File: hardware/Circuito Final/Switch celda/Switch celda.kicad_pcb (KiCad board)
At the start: 2 copper layers, 17 parts, among them Q1 MMBT2222A, Q2 MMBT2907A, Q3 MMBT2222A

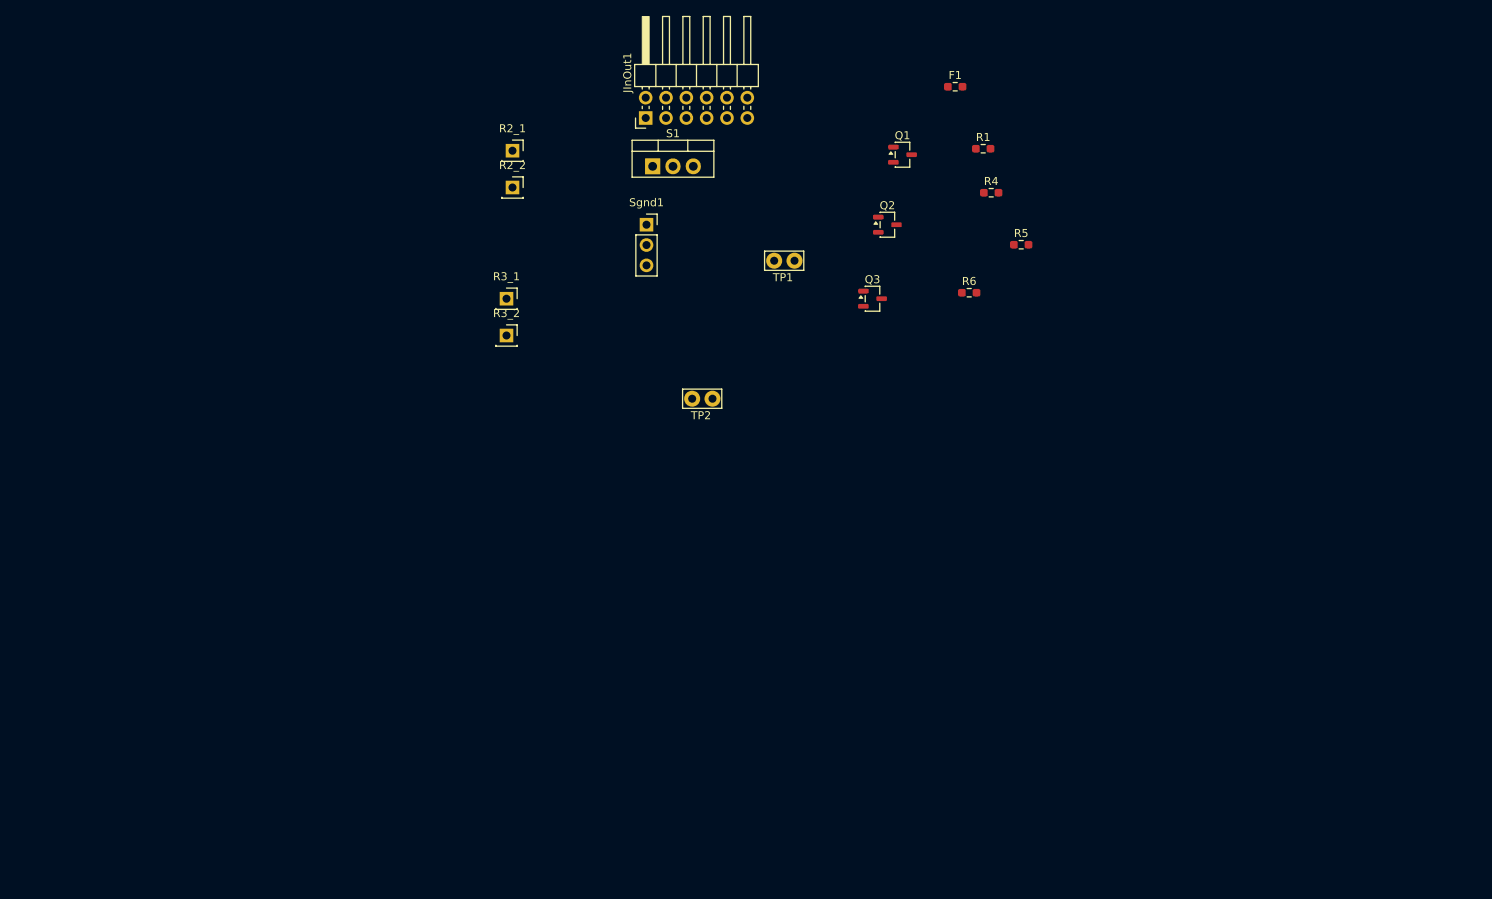
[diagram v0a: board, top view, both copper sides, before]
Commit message: Finalización del esquemático de la celda y subida de datasheets nuevas
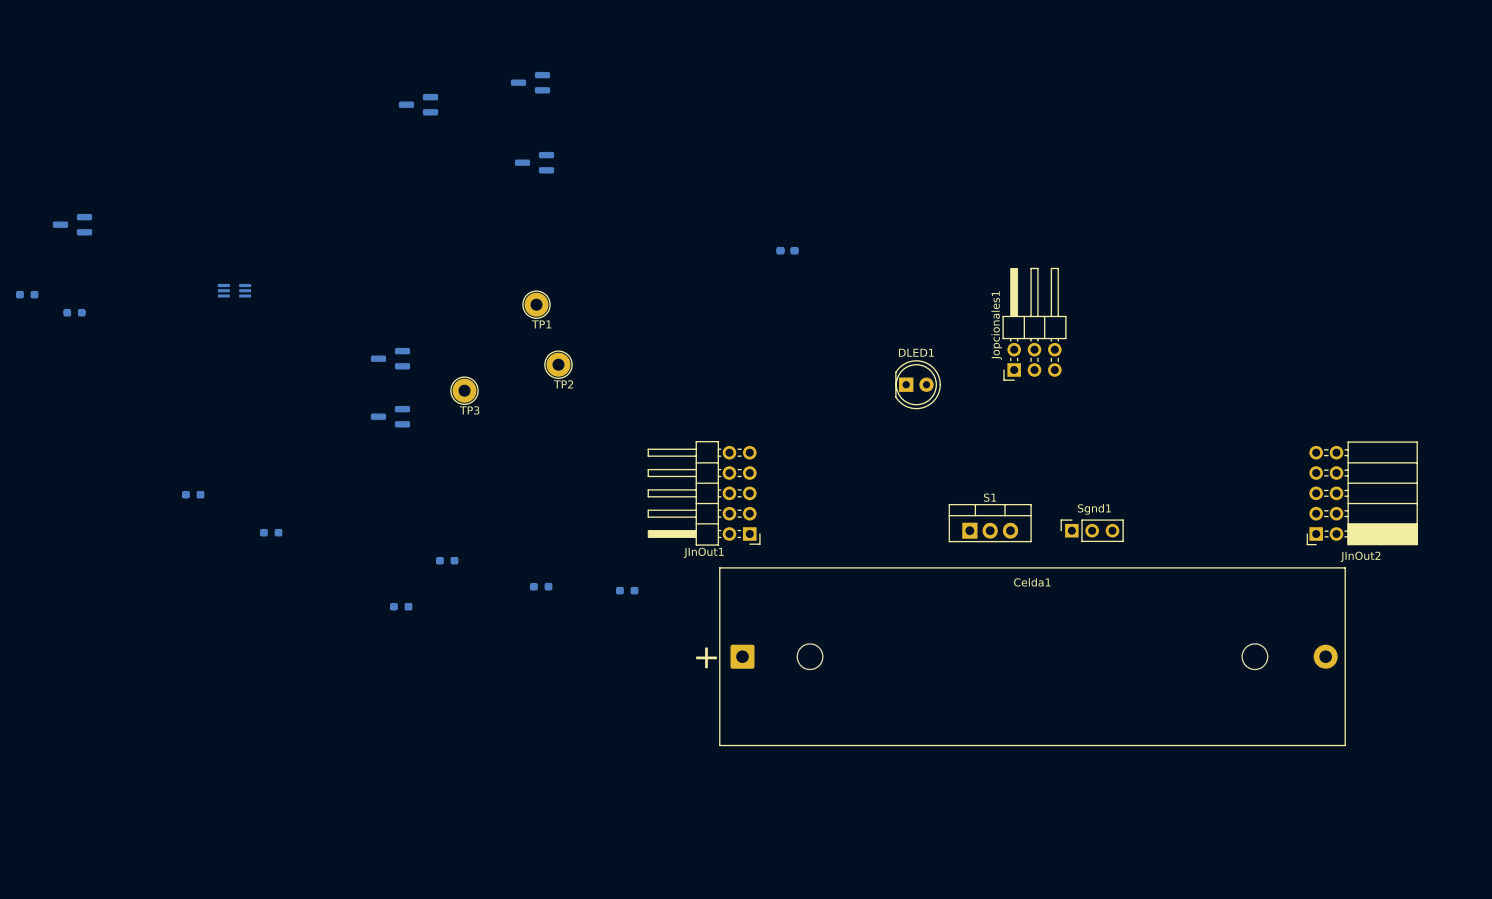
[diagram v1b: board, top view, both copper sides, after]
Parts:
- removed R2_1, R2_2, R3_1, R3_2: Conn_01x01_Socket, Connector_PinSocket_2.54mm:PinSocket_1x01_P2.54mm_Vertical
- added Celda1: Portapilas 18650, Battery:BatteryHolder_MPD_BK-18650-PC2, F.Cu at (143.0, 132.5)
- added DLED1: LED, LED_THT:LED_D5.0mm, F.Cu at (163.5, 98.5)
- added JInOut2: Conn_02x05_Odd_Even, Connector_PinSocket_2.54mm:PinSocket_2x05_P2.54mm_Horizontal, F.Cu at (214.7, 117.2)
- added Jopcionales1: Conn_02x03_Odd_Even, Connector_PinHeader_2.54mm:PinHeader_2x03_P2.54mm_Horizontal, F.Cu at (177.0, 96.7)
- added QLED1: MMBT2222A, Package_TO_SOT_SMD:SOT-23_Handsoldering, B.Cu at (59.2, 78.5)
- added Qinv1: AO3401, Package_TO_SOT_SMD:SOT-23_Handsoldering, B.Cu at (99.0, 95.2)
- added Qinv2: AO3400, Package_TO_SOT_SMD:SOT-23_Handsoldering, B.Cu at (99.0, 102.5)
- added R2: TBD, Resistor_SMD:R_0603_1608Metric_Pad0.98x0.95mm_HandSolder, B.Cu at (84.1, 117.0)
- added R3: TBD, Resistor_SMD:R_0603_1608Metric_Pad0.98x0.95mm_HandSolder, B.Cu at (100.3, 126.2)
- added RLED1: 20k, Resistor_SMD:R_0603_1608Metric_Pad0.98x0.95mm_HandSolder, B.Cu at (59.5, 89.5)
- added RLED2: 1k, Resistor_SMD:R_0603_1608Metric_Pad0.98x0.95mm_HandSolder, B.Cu at (53.6, 87.2)
- added TP3: TP_inv, TestPoint:TestPoint_Loop_D2.54mm_Drill1.5mm_Beaded, F.Cu at (108.2, 99.2)
- added U1: 74LVC1G157, Package_TO_SOT_SMD:SOT-363_SC-70-6_Handsoldering, B.Cu at (79.5, 86.8)
- F1: value Fuse -> ~; footprint Resistor_SMD:R_0603_1608Metric_Pad0.98x0.95mm_HandSolder -> Fuse:Fuse_0603_1608Metric_Pad1.05x0.95mm_HandSolder; moved to B.Cu
- JInOut1: value Conn_02x06_Row_Letter_Last -> Conn_02x05_Odd_Even; footprint Connector_PinHeader_2.54mm:PinHeader_2x06_P2.54mm_Horizontal -> Connector_PinHeader_2.54mm:PinHeader_2x05_P2.54mm_Horizontal
- Q1, Q2, Q3: footprint Package_TO_SOT_SMD:SOT-23-3 -> Package_TO_SOT_SMD:SOT-23_Handsoldering; moved to B.Cu
- R1, R4, R5, R6: moved to B.Cu
- TP1, TP2: footprint TestPoint:TestPoint_Bridge_Pitch2.54mm_Drill1.0mm -> TestPoint:TestPoint_Loop_D2.54mm_Drill1.5mm_Beaded
- moved R1 107.8 mm to (74.3, 112.2), turned to 180 degrees
- moved R4 82.1 mm to (106.1, 120.5), turned to 180 degrees
- moved R5 73.7 mm to (117.8, 123.8), turned to 180 degrees
- moved Sgnd1 65.5 mm to (184.2, 116.8), turned to 90 degrees
- moved Q1 60.8 mm to (102.5, 63.5), turned to 180 degrees
- moved S1 60.4 mm to (171.4, 116.8)
- moved R6 56.7 mm to (128.6, 124.2), turned to 180 degrees
- moved JInOut1 53.6 mm to (143.9, 117.2), turned to 180 degrees
- moved Q2 48.0 mm to (116.5, 60.8), turned to 180 degrees
- moved Q3 45.5 mm to (117.0, 70.8), turned to 180 degrees
- moved TP1 30.2 mm to (117.2, 88.5)
- moved F1 29.3 mm to (148.6, 81.8), turned to 180 degrees
- moved TP2 17.2 mm to (120.0, 96.0)
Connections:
- F1 pad 1: Net-(S1-D) -> Net-(Celda1-+)
- F1 pad 2: bus_neg -> bus_pos
- JInOut1 pad 1: Vcell -> Vcc
- JInOut1 pad 10: bus_neg -> 0
- JInOut1 pad 2: Vcell -> Vcc
- JInOut1 pad 3: Vcell_neg -> Vcell_banco
- JInOut1 pad 4: Vcell_neg -> Vcell_banco
- JInOut1 pad 7: cell_neg -> bus_neg
- JInOut1 pad 8: cell_neg -> bus_neg
- JInOut1 pad 9: bus_neg -> 0
- R1 pad 1: Vcell -> Vin
- R6 pad 1: Vcell_neg -> Net-(Qinv1-D)
- S1 pad 1: Net-(S1-D) -> bus_neg

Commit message: Update PCB celda
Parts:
- moved QLED1 105.2 mm to (143.9, 140.9)
- moved RLED2 102.4 mm to (143.0, 137.1)
- moved Q3 100.5 mm to (190.4, 139.3)
- moved RLED1 99.8 mm to (147.2, 137.2)
- moved Q2 90.7 mm to (177.8, 127.7)
- moved R2 85.0 mm to (168.7, 125.0)
- moved TP3 84.9 mm to (191.3, 117.0)
- moved Q1 84.9 mm to (160.8, 125.2)
- moved Qinv2 80.0 mm to (170.8, 137.8)
- moved R1 78.0 mm to (151.5, 123.8)
- moved Qinv1 77.4 mm to (163.2, 138.3)
- moved U1 73.7 mm to (143.1, 124.1), turned to 0 degrees
- moved TP1 73.1 mm to (184.6, 117.0)
- moved R3 68.4 mm to (168.7, 129.5)
- moved R6 56.6 mm to (183.4, 138.2)
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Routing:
- net Vcell_banco: track 0.00 -> 16.0 mm
- net Vcc: track 0.00 -> 11.1 mm
- net Vcell: track 0.00 -> 10.2 mm
- net Net-(DLED1-K): track 0.00 -> 8.07 mm
- net Net-(QLED1-C): track 0.00 -> 7.68 mm
- net Net-(QLED1-B): track 0.00 -> 5.11 mm
- net bus_pos: track 0.00 -> 5.08 mm
- net bus_neg: track 0.00 -> 5.08 mm
- net 0: track 0.00 -> 5.08 mm
- net cell_neg: track 0.00 -> 2.54 mm
- net Vcell_enable: track 0.00 -> 2.54 mm

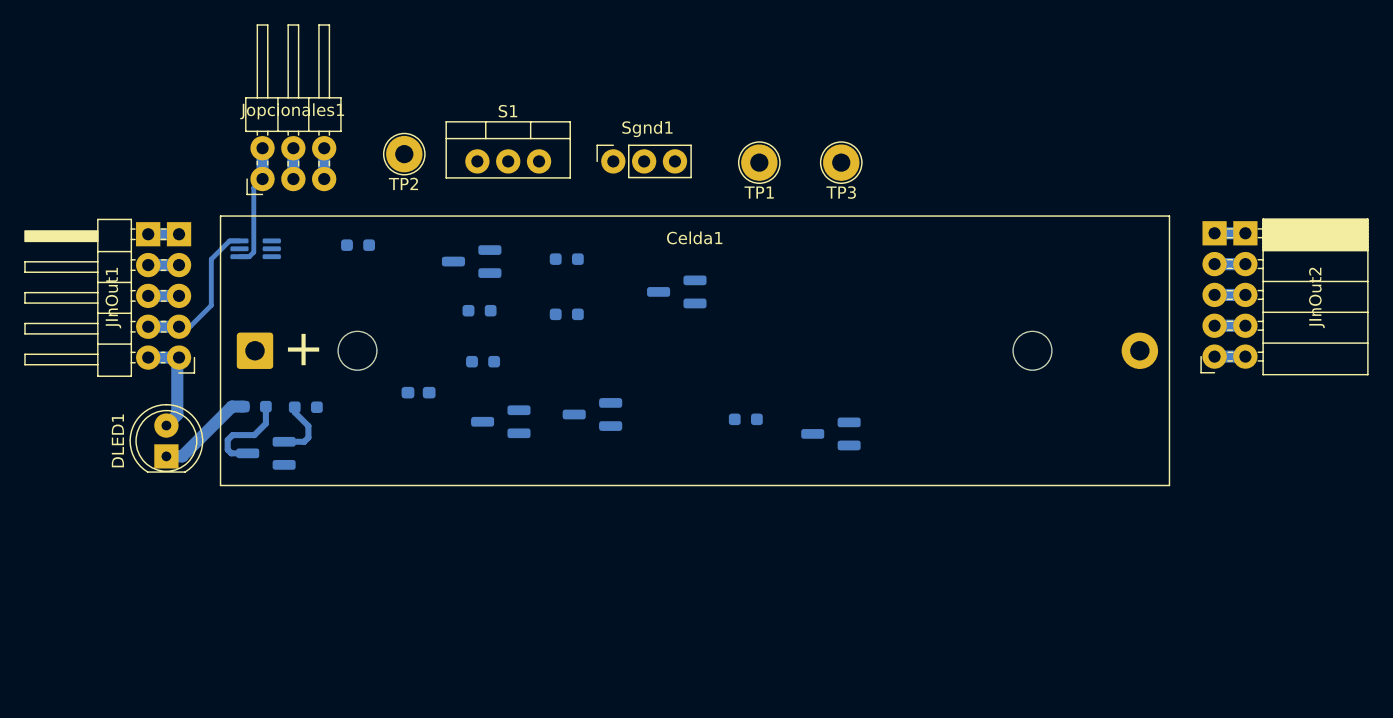
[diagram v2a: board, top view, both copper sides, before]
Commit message: Update PCB celda completo - Revisar integridad
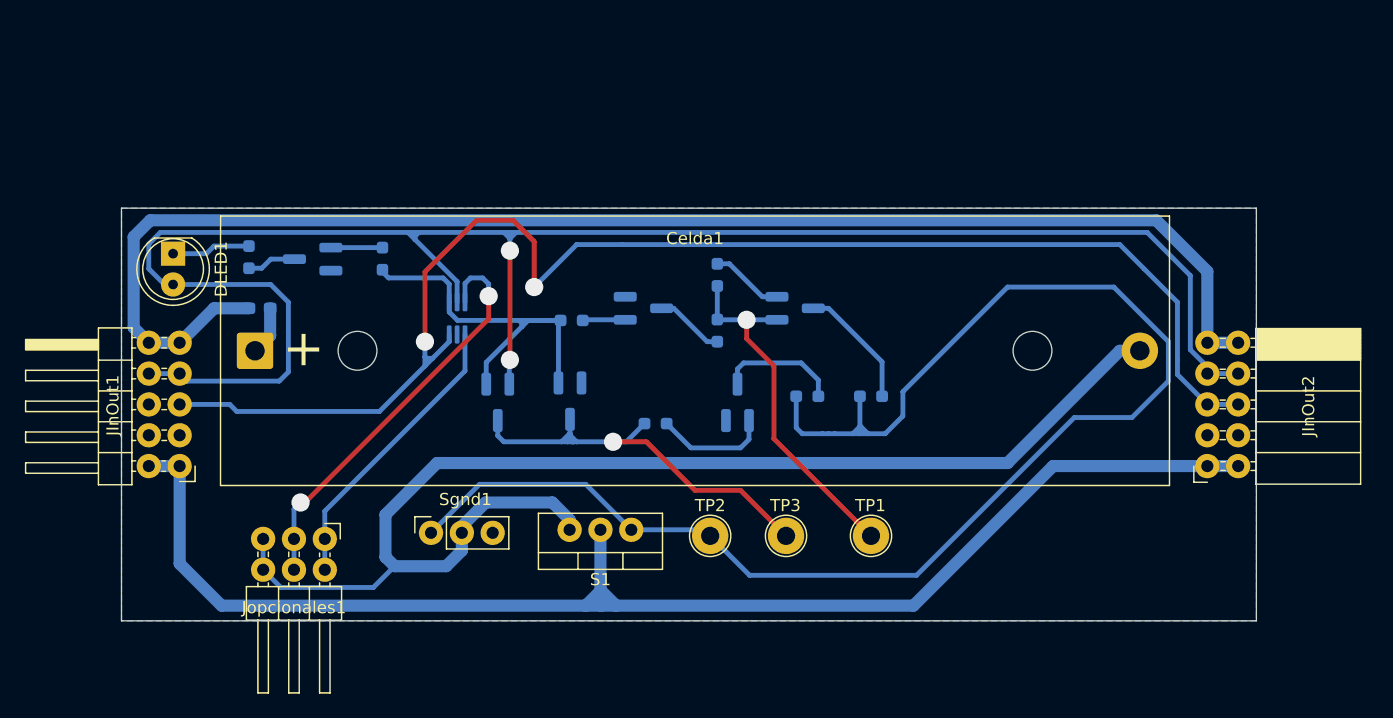
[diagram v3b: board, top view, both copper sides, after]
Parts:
- moved TP2 40.3 mm to (180.5, 147.8), turned to 180 degrees
- moved Sgnd1 34.1 mm to (157.5, 147.5)
- moved R4 33.0 mm to (193.8, 136.2), turned to 0 degrees
- moved S1 32.9 mm to (174.0, 147.2), turned to 180 degrees
- moved TP1 32.1 mm to (193.8, 147.8), turned to 180 degrees
- moved TP3 31.1 mm to (186.8, 147.8), turned to 180 degrees
- moved Jopcionales1 30.1 mm to (148.8, 148.0), turned to -90 degrees
- moved R5 26.9 mm to (188.5, 136.2)
- moved R1 18.7 mm to (169.1, 130.0), turned to 0 degrees
- moved U1 17.6 mm to (159.7, 129.8), turned to 90 degrees
- moved DLED1 16.7 mm to (136.2, 124.5), turned to -90 degrees
- moved QLED1 16.5 mm to (147.8, 125.0)
- moved F1 14.8 mm to (143.4, 129.0)
- moved Q1 14.7 mm to (175.0, 129.0), turned to 0 degrees
- moved RLED1 13.8 mm to (153.5, 124.9), turned to 90 degrees
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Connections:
- JInOut1 pad 1: Vcc -> bus_neg
- JInOut1 pad 10: 0 -> bus_pos
- JInOut1 pad 2: Vcc -> bus_neg
- JInOut1 pad 3: Vcell_banco -> 0
- JInOut1 pad 4: Vcell_banco -> 0
- JInOut1 pad 5: bus_pos -> Vcell_banco
- JInOut1 pad 6: bus_pos -> Vcell_banco
- JInOut1 pad 7: bus_neg -> Vcc
- JInOut1 pad 8: bus_neg -> Vcc
- JInOut1 pad 9: 0 -> bus_pos
- JInOut2 pad 1: Vcc -> bus_neg
- JInOut2 pad 10: 0 -> bus_pos
- JInOut2 pad 2: Vcc -> bus_neg
- JInOut2 pad 3: Vcell_banco -> 0
- JInOut2 pad 4: Vcell_banco -> 0
- JInOut2 pad 5: bus_pos -> Vcell_banco
- JInOut2 pad 6: bus_pos -> Vcell_banco
- JInOut2 pad 7: bus_neg -> Vcc
- JInOut2 pad 8: bus_neg -> Vcc
- JInOut2 pad 9: 0 -> bus_pos
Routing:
- net Vcc: track 11.1 -> 153.4 mm, vias 0 -> 2
- net Net-(S1-G): track 0.00 -> 123.4 mm
- net bus_pos: track 5.08 -> 123.9 mm
- net bus_neg: track 5.08 -> 113.9 mm
- net cell_neg: track 2.54 -> 106.2 mm
- net Vcell_banco: track 16.0 -> 117.5 mm, vias 0 -> 2
- net Net-(Qinv1-D): track 0.00 -> 36.0 mm, vias 0 -> 1
- net Vin: track 0.00 -> 33.0 mm
- net Vcell_enable: track 2.54 -> 34.3 mm, vias 0 -> 2
- net Net-(Q2-B): track 0.00 -> 29.7 mm, vias 0 -> 1
- net Vcell: track 10.2 -> 24.2 mm
- net Net-(Q2-C): track 0.00 -> 10.3 mm
- net Net-(Q3-C): track 0.00 -> 10.0 mm
- net Net-(Q3-B): track 0.00 -> 9.46 mm
- net Net-(Q1-C): track 0.00 -> 5.73 mm
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- added copper zone on B.Cu, net 0
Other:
- board outline added: 93.5 x 34 mm

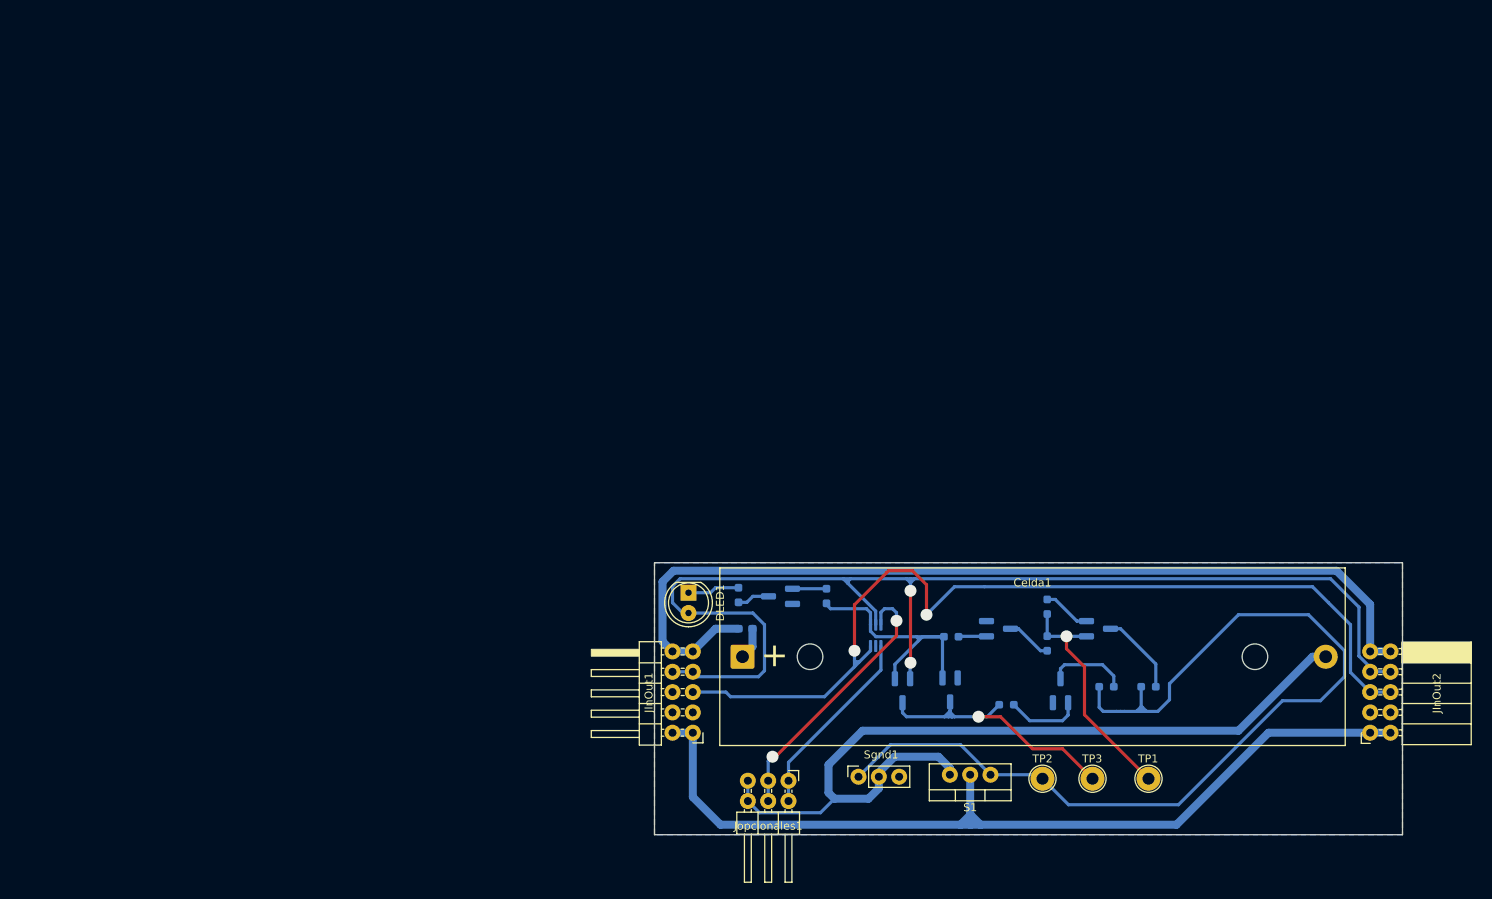
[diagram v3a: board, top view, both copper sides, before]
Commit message: Correcciones menores al plano de tierra
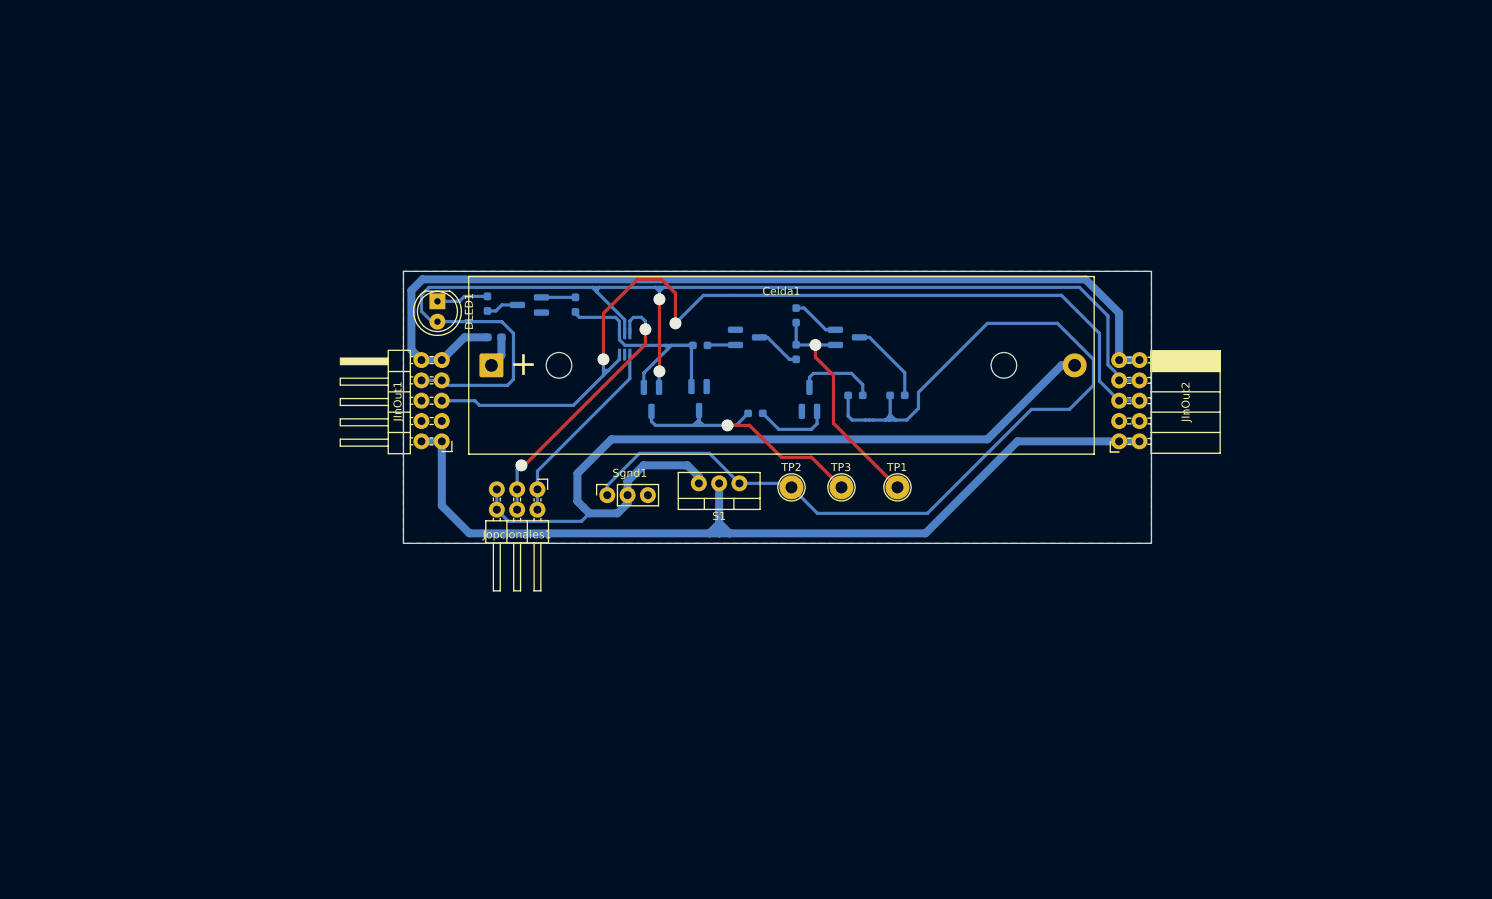
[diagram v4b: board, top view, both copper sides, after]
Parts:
- moved U1 48.1 mm to (128.3, 93.4)
- moved Celda1 48.1 mm to (111.6, 96.1)
- moved DLED1 48.1 mm to (104.9, 88.1)
- moved F1 48.1 mm to (112.0, 92.6)
- moved JInOut1 48.1 mm to (105.4, 105.6)
- moved JInOut2 48.1 mm to (190.1, 105.6)
- moved Jopcionales1 48.1 mm to (117.4, 111.6)
- moved Q1 48.1 mm to (143.6, 92.6)
- moved Q2 48.1 mm to (156.1, 92.6)
- moved Q3 48.1 mm to (151.4, 100.3)
- moved QLED1 48.1 mm to (116.4, 88.5)
- moved Qinv1 48.1 mm to (131.6, 100.3)
- moved Qinv2 48.1 mm to (137.6, 100.2)
- moved R1 48.1 mm to (137.7, 93.6)
- moved R2 48.1 mm to (149.7, 89.8)
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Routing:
- net cell_neg: track 106.2 -> 107.7 mm
- net Net-(S1-G): track 123.4 -> 124.6 mm
